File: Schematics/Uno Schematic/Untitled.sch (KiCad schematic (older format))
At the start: 5 parts

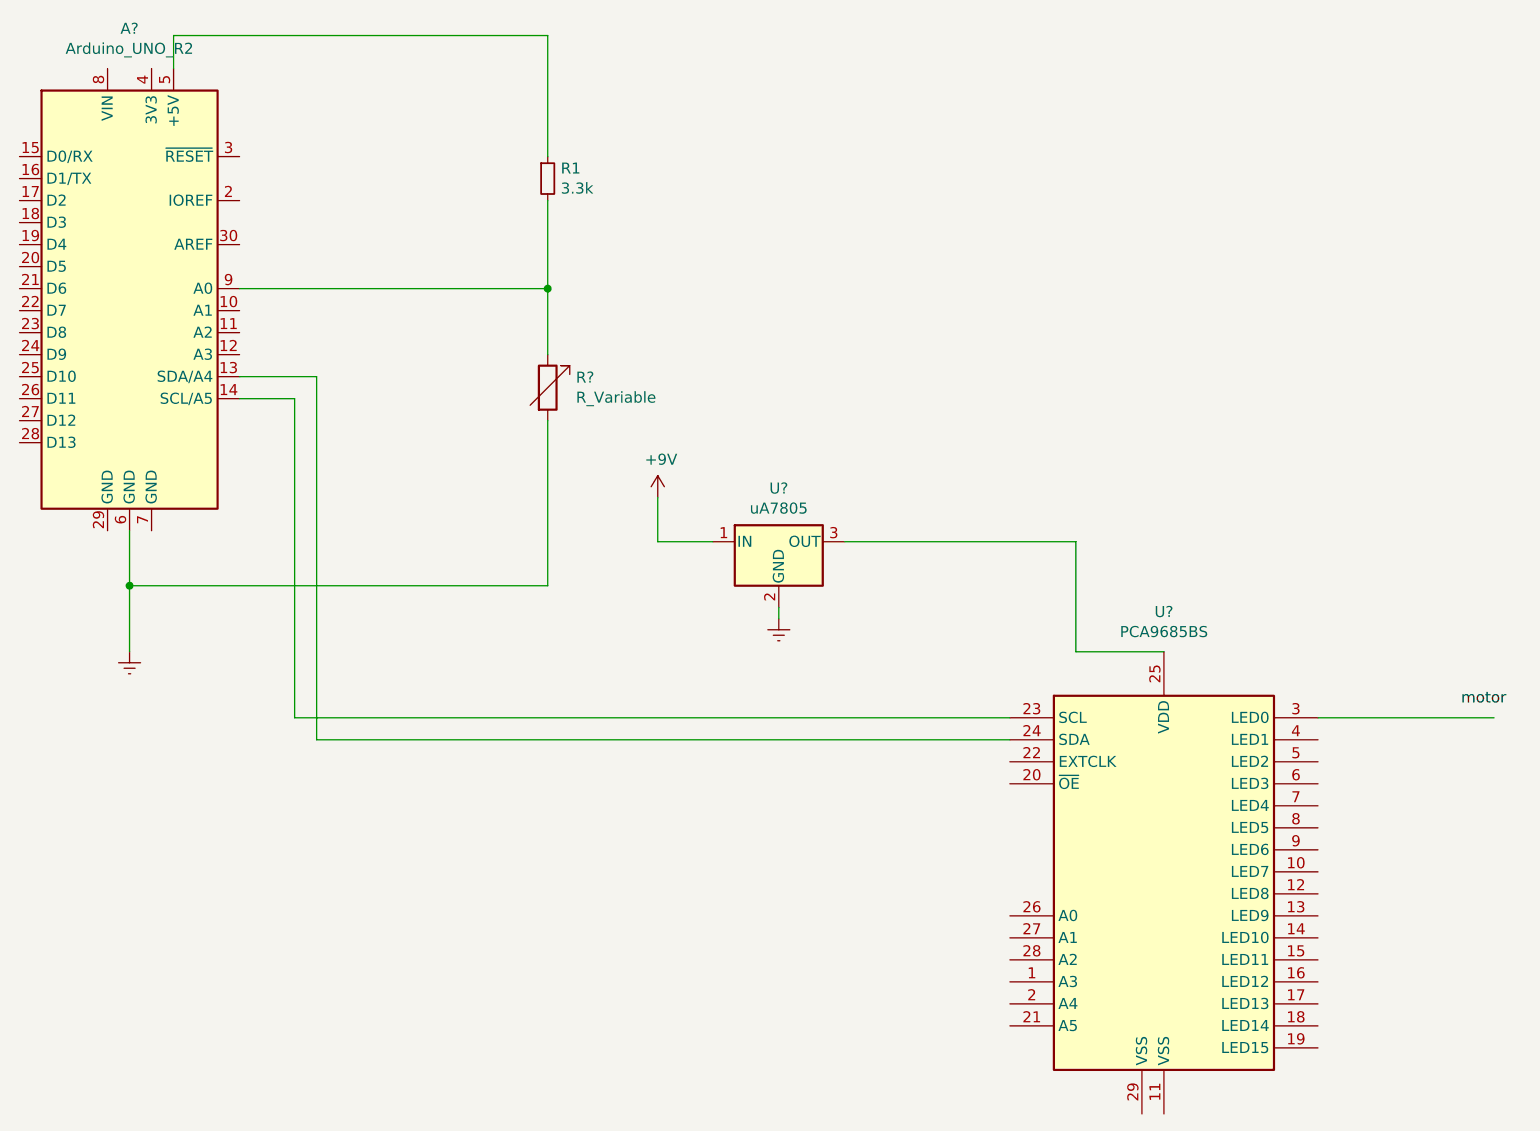
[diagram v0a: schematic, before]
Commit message: updated schematic to include all sensors and motors
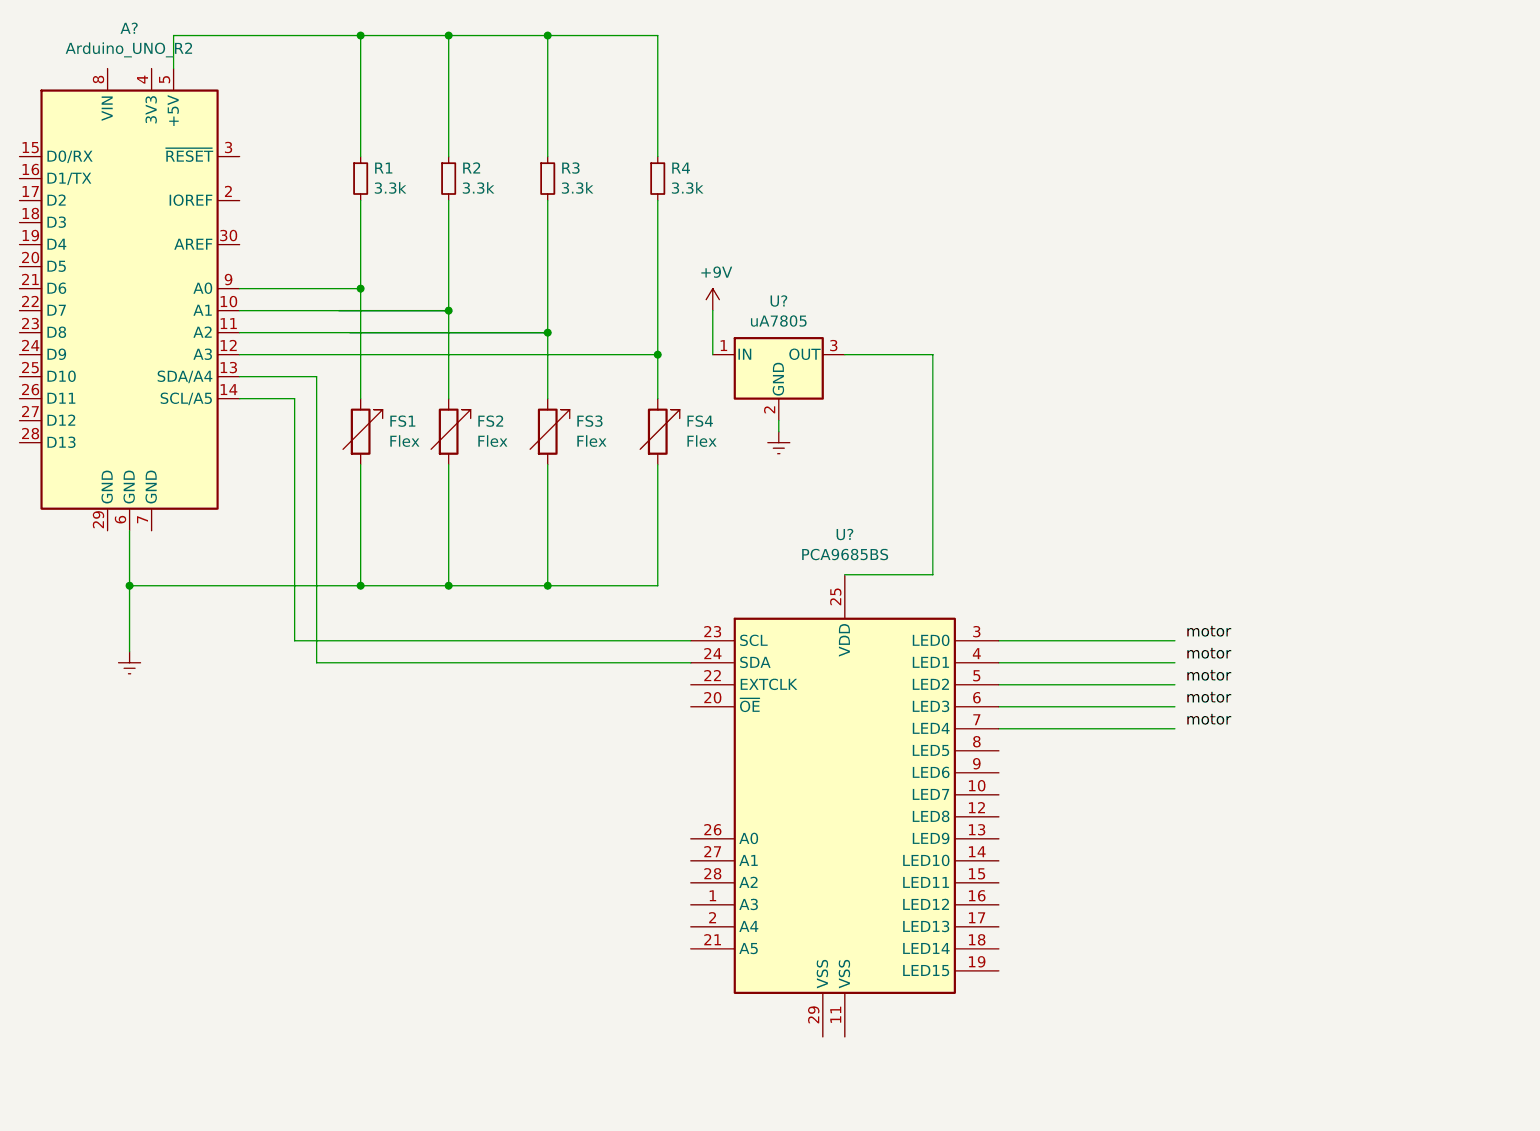
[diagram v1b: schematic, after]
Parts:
- added FS2, FS3, FS4: Flex, symbol Device:R_Variable
- added R2, R3, R4: 3.3k, symbol Device:R_Small
- FS1: renamed from R?; value R_Variable -> Flex
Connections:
- wire segments 23 -> 49
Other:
- moved on the sheet: FS1, R1, U?
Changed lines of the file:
@@
 $EndDescr
-$Comp
-L Driver_LED:PCA9685BS U?
-U 1 1 61AC2446
-P 7700 5000
-F 0 "U?" H 7700 6181 50  0000 C CNN
-F 1 "PCA9685BS" H 7700 6090 50  0000 C CNN
-F 2 "Package_DFN_QFN:QFN-28-1EP_6x6mm_P0.65mm_EP4.25x4.25mm" H 7725 4025 50  0001 L CNN
-F 3 "http://www.nxp.com/documents/data_sheet/PCA9685.pdf" H 7300 5700 50  0001 C CNN
-	1    7700 5000
-	1    0    0    -1
-$EndComp
 $Comp
 L MCU_Module:Arduino_UNO_R2 A?
@@
 $EndComp
 Wire Wire Line
+	3200 1350 3200 1200
+$Comp
+L power:Earth #PWR?
+U 1 1 61AE6891
+P 5950 3000
+F 0 "#PWR?" H 5950 2750 50  0001 C CNN
+F 1 "Earth" H 5950 2850 50  0001 C CNN
+F 2 "" H 5950 3000 50  0001 C CNN
+F 3 "~" H 5950 3000 50  0001 C CNN
+	1    5950 3000
+	1    0    0    -1
+$EndComp
+Wire Wire Line
+	5950 2950 5950 3000
+Text Label 7800 3950 0    50   ~ 0
+motor
+Connection ~ 3000 3700
+Wire Wire Line
+	3000 3700 3000 3450
+Wire Wire Line
 	3000 4000 3000 3700
-Wire Wire Line
-	3200 1350 3200 1200
-Wire Wire Line
-	3200 1200 4900 1200
-Wire Wire Line
-	4900 1200 4900 1750
 $Comp
 L Device:R_Small R1
 U 1 1 61AD0FF0
+P 4050 1850
+F 0 "R1" H 4109 1896 50  0000 L CNN
+F 1 "3.3k" H 4109 1805 50  0000 L CNN
+F 2 "" H 4050 1850 50  0001 C CNN
+F 3 "~" H 4050 1850 50  0001 C CNN
+	1    4050 1850
+	1    0    0    -1
+$EndComp
+Wire Wire Line
+	4050 1200 4050 1750
+Wire Wire Line
+	4050 1950 4050 2350
+Connection ~ 4050 1200
+Wire Wire Line
+	4050 1200 4450 1200
+Wire Wire Line
+	3200 1200 4050 1200
+Wire Wire Line
+	3500 2350 4050 2350
+$Comp
+L Device:R_Small R2
+U 1 1 61AC7A16
+P 4450 1850
+F 0 "R2" H 4509 1896 50  0000 L CNN
+F 1 "3.3k" H 4509 1805 50  0000 L CNN
+F 2 "" H 4450 1850 50  0001 C CNN
+F 3 "~" H 4450 1850 50  0001 C CNN
+	1    4450 1850
+	1    0    0    -1
+$EndComp
+Wire Wire Line
+	4450 1200 4450 1750
+$Comp
+L Device:R_Variable FS2
+U 1 1 61AC9624
+P 4450 3000
+F 0 "FS2" H 4578 3046 50  0000 L CNN
+F 1 "Flex" H 4578 2955 50  0000 L CNN
+F 2 "" V 4380 3000 50  0001 C CNN
+F 3 "~" H 4450 3000 50  0001 C CNN
+	1    4450 3000
+	1    0    0    -1
+$EndComp
+Wire Wire Line
+	4450 1950 4450 2450
+Wire Wire Line
+	3500 2450 4450 2450
+Connection ~ 4450 2450
+$Comp
+L Device:R_Variable FS1
+U 1 1 61AD3804
+P 4050 3000
+F 0 "FS1" H 4178 3046 50  0000 L CNN
+F 1 "Flex" H 4178 2955 50  0000 L CNN
+F 2 "" V 3980 3000 50  0001 C CNN
+F 3 "~" H 4050 3000 50  0001 C CNN
+	1    4050 3000
+	1    0    0    -1
+$EndComp
+Wire Wire Line
+	3000 3700 4050 3700
+Wire Wire Line
+	4050 2350 4050 2850
+Connection ~ 4050 2350
+Wire Wire Line
+	4050 3150 4050 3700
+Connection ~ 4050 3700
+Wire Wire Line
+	4050 3700 4450 3700
+Wire Wire Line
+	4450 2450 4450 2850
+Wire Wire Line
+	4450 3150 4450 3700
+Connection ~ 4450 3700
+Wire Wire Line
+	4450 3700 4900 3700
+$Comp
+L Device:R_Small R3
+U 1 1 61AD281A
 P 4900 1850
-F 0 "R1" H 4959 1896 50  0000 L CNN
+F 0 "R3" H 4959 1896 50  0000 L CNN
 F 1 "3.3k" H 4959 1805 50  0000 L CNN
 F 2 "" H 4900 1850 50  0001 C CNN
@@
 $EndComp
 Wire Wire Line
-	4900 3700 3000 3700
-Connection ~ 3000 3700
-Wire Wire Line
-	3000 3700 3000 3450
-$Comp
-L Device:R_Variable R?
-U 1 1 61AD3804
-P 4900 2800
-F 0 "R?" H 5028 2846 50  0000 L CNN
-F 1 "R_Variable" H 5028 2755 50  0000 L CNN
-F 2 "" V 4830 2800 50  0001 C CNN
-F 3 "~" H 4900 2800 50  0001 C CNN
-	1    4900 2800
-	1    0    0    -1
-$EndComp
-Wire Wire Line
-	4900 2950 4900 3700
-Wire Wire Line
-	4900 1950 4900 2350
-Wire Wire Line
-	3500 2350 4900 2350
-Connection ~ 4900 2350
-Wire Wire Line
-	4900 2350 4900 2650
+	4900 1200 4900 1750
+$Comp
+L Device:R_Variable FS3
+U 1 1 61AD2821
+P 4900 3000
+F 0 "FS3" H 5028 3046 50  0000 L CNN
+F 1 "Flex" H 5028 2955 50  0000 L CNN
+F 2 "" V 4830 3000 50  0001 C CNN
+F 3 "~" H 4900 3000 50  0001 C CNN
+	1    4900 3000
+	1    0    0    -1
+$EndComp
+Wire Wire Line
+	3950 2450 4450 2450
+Wire Wire Line
+	4900 3150 4900 3700
+Wire Wire Line
+	4900 1950 4900 2550
+Wire Wire Line
+	3500 2550 4900 2550
+Connection ~ 4900 2550
+Wire Wire Line
+	4900 2550 4900 2850
+Wire Wire Line
+	5650 2450 5650 2650
+$Comp
+L power:+9V #PWR?
+U 1 1 61AE7E4A
+P 5650 2450
+F 0 "#PWR?" H 5650 2300 50  0001 C CNN
+F 1 "+9V" H 5665 2623 50  0000 C CNN
+F 2 "" H 5650 2450 50  0001 C CNN
+F 3 "" H 5650 2450 50  0001 C CNN
+	1    5650 2450
+	1    0    0    -1
+$EndComp
 $Comp
 L Regulator_Linear:uA7805 U?
 U 1 1 61AD98AF
-P 5950 3500
-F 0 "U?" H 5950 3742 50  0000 C CNN
-F 1 "uA7805" H 5950 3651 50  0000 C CNN
-F 2 "" H 5975 3350 50  0001 L CIN
-F 3 "http://www.ti.com/lit/ds/symlink/ua78.pdf" H 5950 3450 50  0001 C CNN
-	1    5950 3500
-	1    0    0    -1
-$EndComp
-Wire Wire Line
-	7000 4400 3850 4400
-Wire Wire Line
-	3850 4400 3850 2750
-Wire Wire Line
-	3750 2850 3750 4300
-Wire Wire Line
-	3750 4300 7000 4300
-$Comp
-L power:Earth #PWR?
-U 1 1 61AE6891
-P 5950 3850
-F 0 "#PWR?" H 5950 3600 50  0001 C CNN
-F 1 "Earth" H 5950 3700 50  0001 C CNN
-F 2 "" H 5950 3850 50  0001 C CNN
-F 3 "~" H 5950 3850 50  0001 C CNN
-	1    5950 3850
-	1    0    0    -1
-$EndComp
-Wire Wire Line
-	5950 3800 5950 3850
-Wire Wire Line
-	6250 3500 7300 3500
-Wire Wire Line
-	7300 3500 7300 4000
-Wire Wire Line
-	7300 4000 7700 4000
-$Comp
-L power:+9V #PWR?
-U 1 1 61AE7E4A
-P 5400 3300
-F 0 "#PWR?" H 5400 3150 50  0001 C CNN
-F 1 "+9V" H 5415 3473 50  0000 C CNN
-F 2 "" H 5400 3300 50  0001 C CNN
-F 3 "" H 5400 3300 50  0001 C CNN
-	1    5400 3300
-	1    0    0    -1
-$EndComp
-Wire Wire Line
-	5400 3300 5400 3500
-Wire Wire Line
-	5400 3500 5650 3500
-Wire Wire Line
-	8400 4300 9200 4300
-Text Label 9050 4250 0    50   ~ 0
-motor
+P 5950 2650
+F 0 "U?" H 5950 2892 50  0000 C CNN
+F 1 "uA7805" H 5950 2801 50  0000 C CNN
+F 2 "" H 5975 2500 50  0001 L CIN
+F 3 "http://www.ti.com/lit/ds/symlink/ua78.pdf" H 5950 2600 50  0001 C CNN
+	1    5950 2650
+	1    0    0    -1
+$EndComp
+$Comp
+L Device:R_Small R4
+U 1 1 61ADC3C0
+P 5400 1850
+F 0 "R4" H 5459 1896 50  0000 L CNN
+F 1 "3.3k" H 5459 1805 50  0000 L CNN
+F 2 "" H 5400 1850 50  0001 C CNN
+F 3 "~" H 5400 1850 50  0001 C CNN
+	1    5400 1850
+	1    0    0    -1
+$EndComp
+$Comp
+L Device:R_Variable FS4
+U 1 1 61ADC3C7
+P 5400 3000
+F 0 "FS4" H 5528 3046 50  0000 L CNN
+F 1 "Flex" H 5528 2955 50  0000 L CNN
+F 2 "" V 5330 3000 50  0001 C CNN
+F 3 "~" H 5400 3000 50  0001 C CNN
+	1    5400 3000
+	1    0    0    -1
+$EndComp
+Wire Wire Line
+	4000 2550 4900 2550
+Wire Wire Line
+	5400 1950 5400 2650
+Wire Wire Line
+	5400 3150 5400 3700
+Wire Wire Line
+	5400 1200 5400 1750
+Wire Wire Line
+	5400 1200 4900 1200
+Connection ~ 4900 1200
+Connection ~ 4450 1200
+Wire Wire Line
+	4450 1200 4900 1200
+Wire Wire Line
+	5400 3700 4900 3700
+Connection ~ 4900 3700
+Wire Wire Line
+	3500 2650 5400 2650
+Connection ~ 5400 2650
+Wire Wire Line
+	5400 2650 5400 2850
+Wire Wire Line
+	3850 4050 3850 2750
+Wire Wire Line
+	3750 2850 3750 3950
+Text Label 7800 4050 0    50   ~ 0
+motor
+Text Label 7800 4150 0    50   ~ 0
+motor
+Text Label 7800 4250 0    50   ~ 0
+motor
+Text Label 7800 4350 0    50   ~ 0
+motor
+Wire Wire Line
+	6950 4350 7750 4350
+Wire Wire Line
+	6950 4250 7750 4250
+Wire Wire Line
+	6950 4150 7750 4150
+Wire Wire Line
+	6950 4050 7750 4050
+Wire Wire Line
+	6950 3950 7750 3950
+$Comp
+L Driver_LED:PCA9685BS U?
+U 1 1 61AC2446
+P 6250 4650
+F 0 "U?" H 6250 5831 50  0000 C CNN
+F 1 "PCA9685BS" H 6250 5740 50  0000 C CNN
+F 2 "Package_DFN_QFN:QFN-28-1EP_6x6mm_P0.65mm_EP4.25x4.25mm" H 6275 3675 50  0001 L CNN
+F 3 "http://www.nxp.com/documents/data_sheet/PCA9685.pdf" H 5850 5350 50  0001 C CNN
+	1    6250 4650
+	1    0    0    -1
+$EndComp
+Wire Wire Line
+	3850 4050 5550 4050
+Wire Wire Line
+	3750 3950 5550 3950
+Wire Wire Line
+	6250 2650 6650 2650
+Wire Wire Line
+	6650 2650 6650 3650
+Wire Wire Line
+	6650 3650 6250 3650
 $EndSCHEMATC
